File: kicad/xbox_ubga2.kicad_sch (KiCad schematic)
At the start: 1 part, among them U2 uPGA2

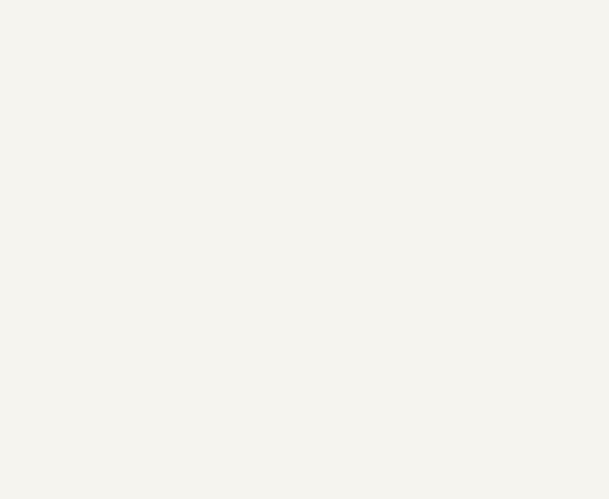
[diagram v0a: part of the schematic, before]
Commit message: Rev 3.1:  - change via's to 0.3mm drill/0.4mm ring for cheaper manufacturing  - add leveling 0603 resistors on backside in the corners to prevent PCB tilt during reflow
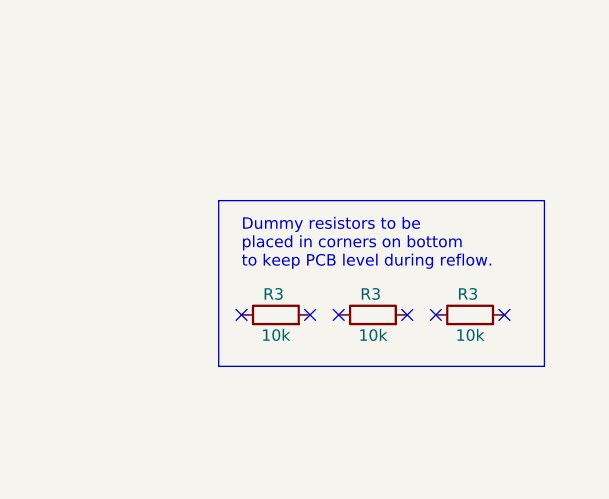
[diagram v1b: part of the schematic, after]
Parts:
- added R3 (x3): 10k, Resistor_SMD:R_0603_1608Metric, symbol Device:R
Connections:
- no-connect marks 34 -> 40
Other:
- note added: "Dummy resistors to be placed in corners on bottom to keep PCB level during reflow."
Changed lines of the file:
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@@
   (no_connect (at 53.34 97.536))
   (no_connect (at 113.03 70.485))
+  (no_connect (at 145.415 136.525))
   (no_connect (at 76.2 131.826))
   (no_connect (at 53.34 138.176))
   (no_connect (at 53.34 83.566))
+  (no_connect (at 134.62 136.525))
+  (no_connect (at 116.205 136.525))
   (no_connect (at 113.03 69.215))
   (no_connect (at 53.34 87.376))
+  (no_connect (at 137.795 136.525))
   (no_connect (at 113.03 85.725))
   (no_connect (at 53.34 105.156))
+  (no_connect (at 123.825 136.525))
   (no_connect (at 113.03 57.785))
   (no_connect (at 113.03 84.455))
@@
   (no_connect (at 135.89 90.805))
   (no_connect (at 53.34 125.476))
+  (no_connect (at 127 136.525))
   (no_connect (at 76.2 133.096))
   (no_connect (at 113.03 61.595))
@@
     (stroke (width 0) (type default))
   )
+  (rectangle (start 113.665 123.825) (end 149.86 142.24)
+    (stroke (width 0) (type default))
+    (fill (type none))
+  )
+  (text "Dummy resistors to be\nplaced in corners on bottom\nto keep PCB level during reflow."
+    (at 116.205 131.445 0)
+    (effects (font (size 1.27 1.27)) (justify left bottom))
+  )
   (global_label "RTTIMPEDP" (shape input) (at 106.045 71.755 180) (fields_autoplaced)
     (effects (font (size 0.4 0.4)) (justify right))
@@
     )
   )
+  (symbol (lib_id "Device:R") (at 130.81 136.525 90) (unit 1)
+    (in_bom yes) (on_board yes) (dnp no)
+    (property "Reference" "R3" (at 130.556 134.239 90)
+      (effects (font (size 1.27 1.27)))
+    )
+    (property "Value" "10k" (at 130.81 138.811 90)
+      (effects (font (size 1.27 1.27)))
+    )
+    (property "Footprint" "Resistor_SMD:R_0603_1608Metric" (at 130.81 138.303 90)
+      (effects (font (size 1.27 1.27)) hide)
+    )
+    (property "Datasheet" "~" (at 130.81 136.525 0)
+      (effects (font (size 1.27 1.27)) hide)
+    )
+    (pin "1")
+    (pin "2")
+    (instances
+      (project "interposer"
+        (path "/ec820575-024d-42cb-bfa5-b230176ba695/cfd51080-4f1a-4877-b9f2-49ef7842424e"
+          (reference "R3") (unit 1)
+        )
+        (path "/ec820575-024d-42cb-bfa5-b230176ba695/91f8d4ec-ae32-44bd-8462-8bb796df34a6"
+          (reference "R6") (unit 1)
+        )
+      )
+    )
+  )
   (symbol (lib_id "power:GND") (at 141.605 60.96 0) (unit 1)
     (in_bom yes) (on_board yes) (dnp no) (fields_autoplaced)
@@
         (path "/ec820575-024d-42cb-bfa5-b230176ba695/91f8d4ec-ae32-44bd-8462-8bb796df34a6"
           (reference "#PWR02") (unit 1)
+        )
+      )
+    )
+  )
+  (symbol (lib_id "Device:R") (at 141.605 136.525 90) (unit 1)
+    (in_bom yes) (on_board yes) (dnp no)
+    (property "Reference" "R3" (at 141.351 134.239 90)
+      (effects (font (size 1.27 1.27)))
+    )
+    (property "Value" "10k" (at 141.605 138.811 90)
+      (effects (font (size 1.27 1.27)))
+    )
+    (property "Footprint" "Resistor_SMD:R_0603_1608Metric" (at 141.605 138.303 90)
+      (effects (font (size 1.27 1.27)) hide)
+    )
+    (property "Datasheet" "~" (at 141.605 136.525 0)
+      (effects (font (size 1.27 1.27)) hide)
+    )
+    (pin "1")
+    (pin "2")
+    (instances
+      (project "interposer"
+        (path "/ec820575-024d-42cb-bfa5-b230176ba695/cfd51080-4f1a-4877-b9f2-49ef7842424e"
+          (reference "R3") (unit 1)
+        )
+        (path "/ec820575-024d-42cb-bfa5-b230176ba695/91f8d4ec-ae32-44bd-8462-8bb796df34a6"
+          (reference "R7") (unit 1)
         )
       )
@@
         )
       )
+    )
+  )
+  (symbol (lib_id "Device:R") (at 120.015 136.525 90) (unit 1)
+    (in_bom yes) (on_board yes) (dnp no)
+    (property "Reference" "R3" (at 119.761 134.239 90)
+      (effects (font (size 1.27 1.27)))
+    )
+    (property "Value" "10k" (at 120.015 138.811 90)
+      (effects (font (size 1.27 1.27)))
+    )
+    (property "Footprint" "Resistor_SMD:R_0603_1608Metric" (at 120.015 138.303 90)
+      (effects (font (size 1.27 1.27)) hide)
+    )
+    (property "Datasheet" "~" (at 120.015 136.525 0)
+      (effects (font (size 1.27 1.27)) hide)
+    )
+    (pin "1")
+    (pin "2")
+    (instances
+      (project "interposer"
+        (path "/ec820575-024d-42cb-bfa5-b230176ba695/cfd51080-4f1a-4877-b9f2-49ef7842424e"
+          (reference "R3") (unit 1)
+        )
+        (path "/ec820575-024d-42cb-bfa5-b230176ba695/91f8d4ec-ae32-44bd-8462-8bb796df34a6"
+          (reference "R5") (unit 1)
+        )
+      )

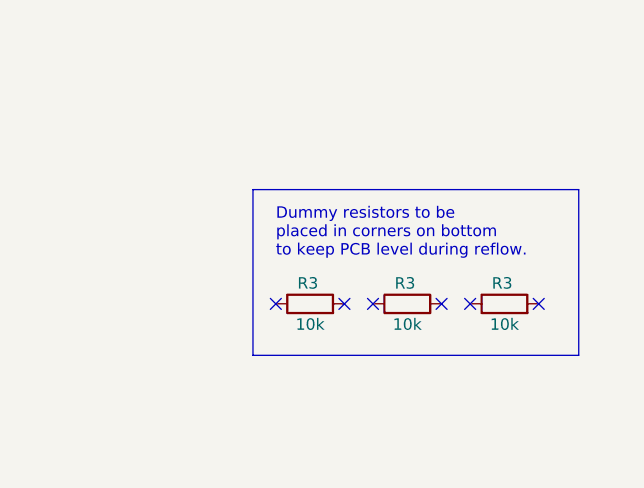
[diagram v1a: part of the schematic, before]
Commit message: Revision 3.2
Implement fixes that allow interposer to be actually functional for the first time:
 - Fix uBGA495 pin P1 from VTT --> VCC since this is VCC on xbox motherboard.
 - Fix P370 pin AJ3 (RESET2#) from GND --> NC.

Furthermore, pins AL1 (reserved), AK36 (VID output), AF36 (DETECT) now left NC instead of connected to GND.

Outline slightly trimmed near bottom to provide some clearance against a cap on 1.6 motherboards.

Design specs loosened, from 4 mil tracks/4 mil clearance/0.3mm drills --> 5 mil/5 mil/0.3mm.

Board thickness recommendation is now 1.6mm instead of 1.2mm for additional rigidity.
Trace lengths now matched at 27.0mm (was 25.0mm).

Added BGA footprint indicator on front silkscreen.
Added BGA pin numbering on back silkscreen.
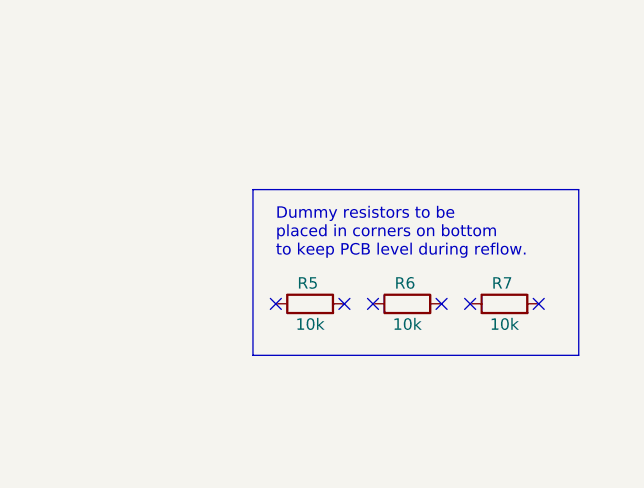
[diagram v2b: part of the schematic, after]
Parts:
- renumbered R3 to R5, R3 to R6, R3 to R7
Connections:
- net VCC: now also U2.P1 (VCC)
- net VCCT: no longer U2.P1 (VCCT)
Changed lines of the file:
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@@
   (symbol (lib_id "Device:R") (at 130.81 136.525 90) (unit 1)
     (in_bom yes) (on_board yes) (dnp no)
-    (property "Reference" "R3" (at 130.556 134.239 90)
+    (property "Reference" "R6" (at 130.556 134.239 90)
       (effects (font (size 1.27 1.27)))
     )
@@
     (instances
       (project "interposer"
-        (path "/ec820575-024d-42cb-bfa5-b230176ba695/cfd51080-4f1a-4877-b9f2-49ef7842424e"
-          (reference "R3") (unit 1)
-        )
         (path "/ec820575-024d-42cb-bfa5-b230176ba695/91f8d4ec-ae32-44bd-8462-8bb796df34a6"
           (reference "R6") (unit 1)
@@
   (symbol (lib_id "Device:R") (at 141.605 136.525 90) (unit 1)
     (in_bom yes) (on_board yes) (dnp no)
-    (property "Reference" "R3" (at 141.351 134.239 90)
+    (property "Reference" "R7" (at 141.351 134.239 90)
       (effects (font (size 1.27 1.27)))
     )
@@
     (instances
       (project "interposer"
-        (path "/ec820575-024d-42cb-bfa5-b230176ba695/cfd51080-4f1a-4877-b9f2-49ef7842424e"
-          (reference "R3") (unit 1)
-        )
         (path "/ec820575-024d-42cb-bfa5-b230176ba695/91f8d4ec-ae32-44bd-8462-8bb796df34a6"
           (reference "R7") (unit 1)
@@
   (symbol (lib_id "Device:R") (at 120.015 136.525 90) (unit 1)
     (in_bom yes) (on_board yes) (dnp no)
-    (property "Reference" "R3" (at 119.761 134.239 90)
+    (property "Reference" "R5" (at 119.761 134.239 90)
       (effects (font (size 1.27 1.27)))
     )
@@
     (instances
       (project "interposer"
-        (path "/ec820575-024d-42cb-bfa5-b230176ba695/cfd51080-4f1a-4877-b9f2-49ef7842424e"
-          (reference "R3") (unit 1)
-        )
         (path "/ec820575-024d-42cb-bfa5-b230176ba695/91f8d4ec-ae32-44bd-8462-8bb796df34a6"
           (reference "R5") (unit 1)

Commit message: Rev. 3.3, minor changes:  - Resistor network RN01 changed to 4 distinct 0603's since people continuously order an incorrect part  - Height of interposer slightly reduced by 0.3mm on both top and bottom. on top, the pins for standard mounting bracket require less trimming. On bottom there is less obstruction with C1D5 on xbox motherboard.  - Added xbox.munia.io branding on the bottom silk  - Align tool modified accordingly.
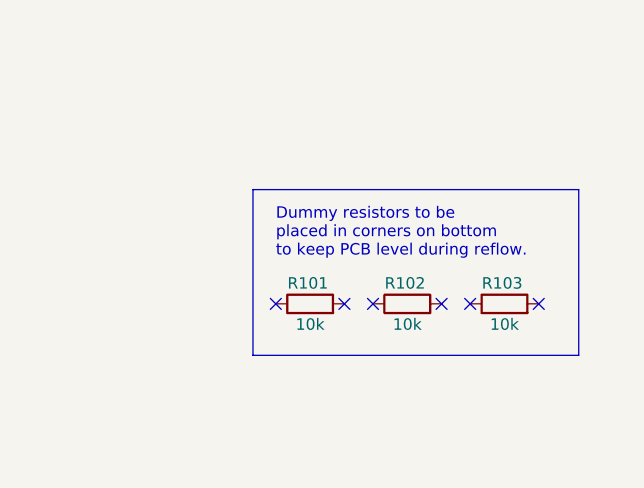
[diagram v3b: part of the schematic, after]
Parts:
- U2: now left out of the parts list
- renumbered R5 to R101, R6 to R102, R7 to R103
